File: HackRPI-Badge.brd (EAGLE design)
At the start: 124.5 x 94 mm, 41 parts, among them J1 FTDI_BASICPTH, J2 SOLDERJUMPERTRACE-PTH, U2 3.3V, U4 74595, U5 74595, U6 74595, U7 74165DT

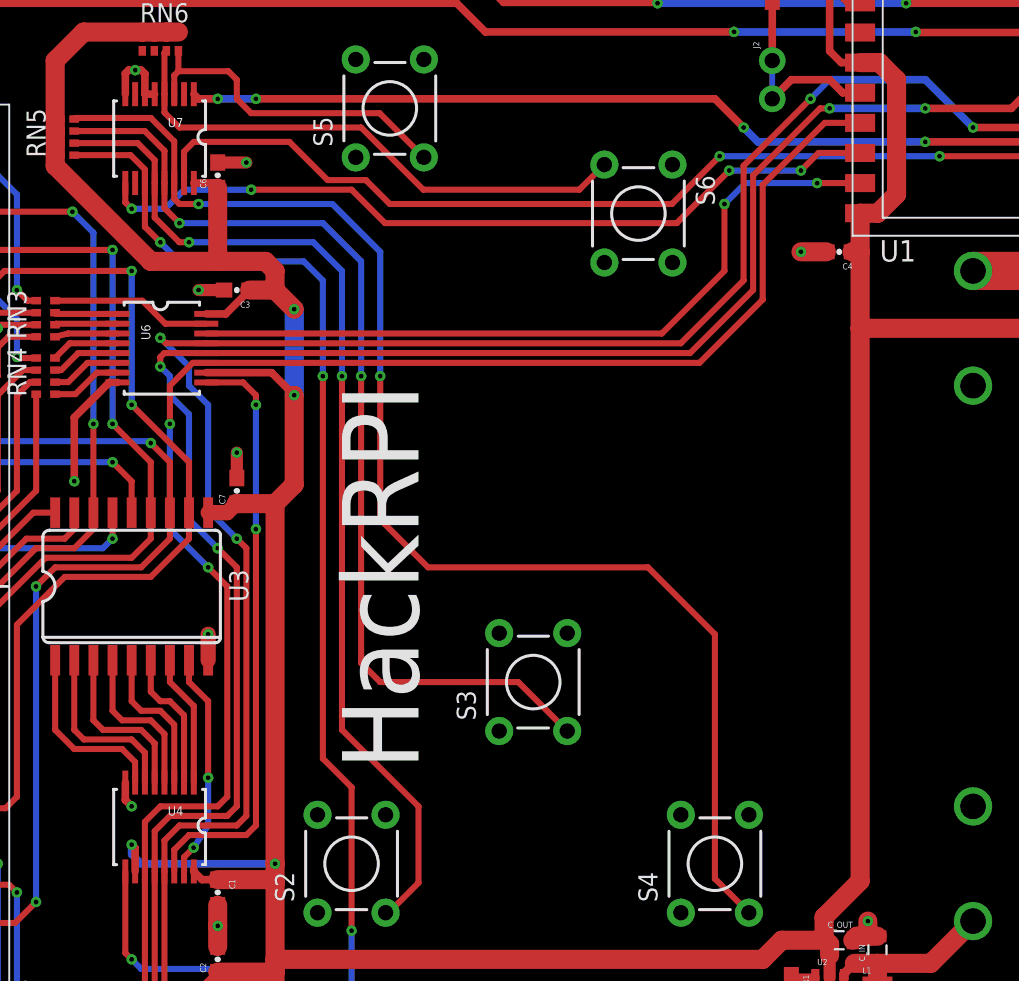
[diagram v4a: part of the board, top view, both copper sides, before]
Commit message: Added flash memory for storing certificates, named some nets to be more clear
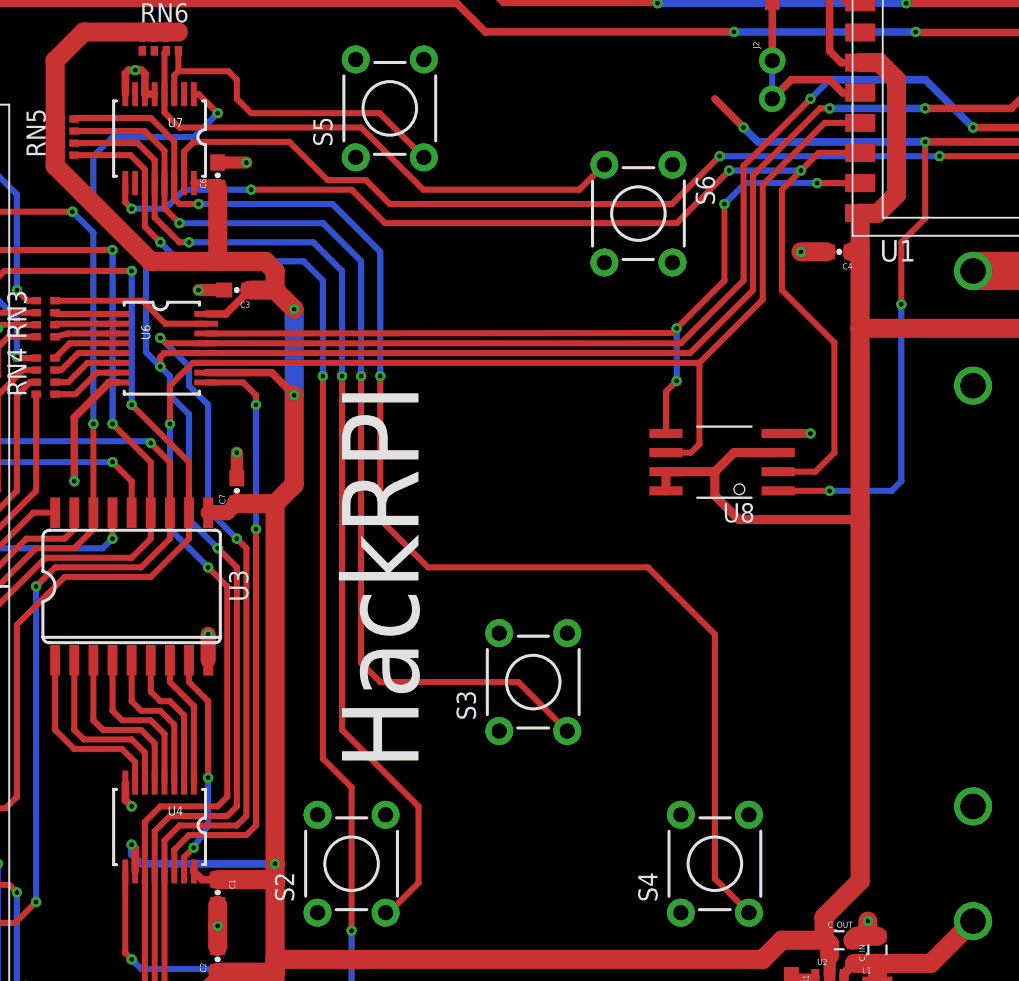
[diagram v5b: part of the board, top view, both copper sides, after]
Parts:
- added U8: AT25FS010, SparkFun-DigitalIC:SO08WIDE
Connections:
- net GPIO2 renamed INPUT_CS
- removed net GPIO0: R3.1, U1.12, U7.1
- new net FLASH_CS: R3.1, U1.12, U8.1
- net 3.3V: now also U8.3, U8.7, U8.8
- net GND: now also U8.4
- net LAT: now also U7.1
- net MISO: now also U8.2
- net MOSI: now also U8.5
- net SCK: now also U8.6
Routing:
- net GPIO0: track 64.9 -> 0.00 mm, vias 4 -> 0
- net FLASH_CS: track 0.00 -> 62.8 mm, vias 0 -> 4
- net LAT: track 128.7 -> 156.1 mm, vias 4 -> 5
- net MISO: track 53.6 -> 78.6 mm
- net 3.3V: track 284.5 -> 305.9 mm
- net SCK: track 111.1 -> 118.9 mm
- net MOSI: track 50.2 -> 57.8 mm, vias 2 -> 4
- net GND: track 36.6 -> 38.7 mm, vias 13 -> 14
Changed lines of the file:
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@@
 <attribute name="PROD_ID" value="BATT-08571" x="116.84" y="45.72" size="1.778" layer="28" rot="MR270" display="off"/>
 </element>
+<element name="U8" library="SparkFun-DigitalIC" package="SO08WIDE" value="AT25FS010" x="91.44" y="54.61" rot="R90"/>
 </elements>
 <signals>
@@
 <wire x1="54.61" y1="59.69" x2="56.125" y2="61.205" width="0.4064" layer="1"/>
 <wire x1="56.125" y1="61.205" x2="57.025" y2="61.205" width="0.4064" layer="1"/>
+<contactref element="U8" pad="6"/>
+<wire x1="87.5538" y1="55.245" x2="89.2175" y2="55.245" width="0.4064" layer="1"/>
+<wire x1="89.78" y1="61.205" x2="89.78" y2="55.8075" width="0.4064" layer="1"/>
+<wire x1="89.78" y1="55.8075" x2="89.2175" y2="55.245" width="0.4064" layer="1"/>
 </signal>
 <signal name="MISO">
@@
 <wire x1="96.52" y1="73.9775" x2="97.6875" y2="75.145" width="0.4064" layer="1"/>
 <wire x1="97.6875" y1="75.145" x2="100.45" y2="75.145" width="0.4064" layer="1"/>
+<contactref element="U8" pad="2"/>
+<wire x1="95.0087" y1="53.975" x2="97.4725" y2="53.975" width="0.4064" layer="1"/>
+<wire x1="97.4725" y1="53.975" x2="98.7425" y2="55.245" width="0.4064" layer="1"/>
+<wire x1="98.7425" y1="55.245" x2="98.7425" y2="62.5475" width="0.4064" layer="1"/>
+<wire x1="98.7425" y1="62.5475" x2="95.25" y2="66.04" width="0.4064" layer="1"/>
+<wire x1="95.25" y1="66.04" x2="95.25" y2="72.7075" width="0.4064" layer="1"/>
+<wire x1="95.25" y1="72.7075" x2="96.52" y2="73.9775" width="0.4064" layer="1"/>
 </signal>
 <signal name="MOSI">
 <contactref element="U1" pad="7"/>
 <contactref element="U6" pad="14"/>
-<wire x1="57.025" y1="63.155" x2="87.285" y2="63.155" width="0.4064" layer="1"/>
-<wire x1="87.285" y1="63.155" x2="91.44" y2="67.31" width="0.4064" layer="1"/>
-<wire x1="91.44" y1="67.31" x2="91.44" y2="71.755" width="0.4064" layer="1"/>
+<wire x1="57.025" y1="63.155" x2="87.9475" y2="63.1825" width="0.4064" layer="1"/>
+<wire x1="87.9475" y1="63.1825" x2="88.265" y2="63.5" width="0.4064" layer="1"/>
+<wire x1="88.265" y1="63.5" x2="91.44" y2="66.675" width="0.4064" layer="1"/>
+<wire x1="91.44" y1="66.675" x2="91.44" y2="71.755" width="0.4064" layer="1"/>
 <via x="91.44" y="71.755" extent="1-16" drill="0.3048"/>
 <wire x1="91.44" y1="71.755" x2="92.83" y2="73.145" width="0.4064" layer="16"/>
@@
 <via x="97.5925" y="73.145" extent="1-16" drill="0.3048"/>
 <wire x1="97.5925" y1="73.145" x2="92.83" y2="73.145" width="0.4064" layer="16"/>
+<contactref element="U8" pad="5"/>
+<wire x1="87.5538" y1="59.2963" x2="87.5538" y2="56.515" width="0.4064" layer="1"/>
+<wire x1="88.265" y1="63.5" x2="88.265" y2="60.0075" width="0.4064" layer="16"/>
+<via x="88.265" y="60.0075" extent="1-16" drill="0.3048"/>
+<wire x1="88.265" y1="60.0075" x2="87.5538" y2="59.2963" width="0.4064" layer="1"/>
+<via x="88.265" y="63.5" extent="1-16" drill="0.3048"/>
 </signal>
 <signal name="3.3V" class="1">
@@
 <wire x1="98.425" y1="21.855" x2="98.425" y2="20.3501" width="0.8128" layer="1"/>
 <wire x1="98.055" y1="24.395" x2="100.45" y2="26.79" width="1.27" layer="1"/>
-<wire x1="100.45" y1="26.79" x2="100.45" y2="63.5" width="1.27" layer="1"/>
+<wire x1="100.45" y1="26.79" x2="100.45" y2="50.4825" width="1.27" layer="1"/>
+<wire x1="100.45" y1="50.4825" x2="100.45" y2="63.5" width="1.27" layer="1"/>
 <wire x1="100.45" y1="63.5" x2="100.45" y2="68.58" width="1.27" layer="1"/>
 <wire x1="100.45" y1="68.58" x2="100.45" y2="71.145" width="1.27" layer="1"/>
@@
 <wire x1="57.025" y1="60.555" x2="61.365" y2="60.555" width="0.508" layer="1"/>
 <wire x1="61.365" y1="60.555" x2="62.865" y2="59.055" width="0.508" layer="1"/>
+<contactref element="U8" pad="3"/>
+<contactref element="U8" pad="8"/>
+<contactref element="U8" pad="7"/>
+<wire x1="87.5538" y1="52.705" x2="87.5538" y2="53.975" width="0.6096" layer="1"/>
+<wire x1="87.5538" y1="53.975" x2="90.805" y2="53.975" width="0.6096" layer="1"/>
+<wire x1="95.0087" y1="55.245" x2="92.075" y2="55.245" width="0.6096" layer="1"/>
+<wire x1="92.075" y1="55.245" x2="90.805" y2="53.975" width="0.6096" layer="1"/>
+<wire x1="90.805" y1="53.975" x2="90.805" y2="52.3875" width="0.6096" layer="1"/>
+<wire x1="90.805" y1="52.3875" x2="92.3925" y2="50.8" width="0.6096" layer="1"/>
+<wire x1="100.45" y1="50.8" x2="92.3925" y2="50.8" width="0.6096" layer="1"/>
+<wire x1="100.45" y1="50.8" x2="100.45" y2="50.4825" width="0.6096" layer="1"/>
 </signal>
 <signal name="GND" class="1">
@@
 <wire x1="48.26" y1="57.58" x2="48.26" y2="53.34" width="0.508" layer="1"/>
 <via x="48.26" y="53.34" extent="1-16" drill="0.3048"/>
-</signal>
-<signal name="GPIO2">
+<contactref element="U8" pad="4"/>
+<wire x1="95.0087" y1="56.515" x2="97.155" y2="56.515" width="0.6096" layer="1"/>
+<via x="97.155" y="56.515" extent="1-16" drill="0.3048"/>
+</signal>
+<signal name="INPUT_CS">
 <contactref element="U1" pad="11"/>
 <contactref element="R4" pad="1"/>
-<contactref element="U7" pad="15"/>
 <wire x1="115.45" y1="75.145" x2="118.95" y2="75.145" width="0.8128" layer="1"/>
 <wire x1="118.95" y1="75.145" x2="119.165" y2="74.93" width="0.8128" layer="1"/>
-<wire x1="55.55" y1="73.15" x2="55.55" y2="75.235" width="0.4064" layer="1"/>
 <wire x1="55.55" y1="75.235" x2="56.1975" y2="75.8825" width="0.4064" layer="1"/>
 <wire x1="56.1975" y1="75.8825" x2="62.5475" y2="75.8825" width="0.4064" layer="1"/>
@@
 <wire x1="112.395" y1="74.93" x2="112.61" y2="75.145" width="0.4064" layer="1"/>
 <wire x1="112.61" y1="75.145" x2="115.45" y2="75.145" width="0.4064" layer="1"/>
-</signal>
-<signal name="GPIO0">
+<contactref element="U7" pad="15"/>
+<wire x1="55.55" y1="75.235" x2="55.55" y2="73.15" width="0.4064" layer="1"/>
+</signal>
+<signal name="FLASH_CS">
 <contactref element="U1" pad="12"/>
 <contactref element="R3" pad="1"/>
-<contactref element="U7" pad="1"/>
-<wire x1="56.51" y1="78.74" x2="57.785" y2="78.74" width="0.508" layer="1"/>
-<via x="57.785" y="78.74" extent="1-16" drill="0.3048"/>
-<wire x1="57.785" y1="78.74" x2="60.325" y2="78.74" width="0.508" layer="16"/>
-<via x="60.325" y="78.74" extent="1-16" drill="0.3048"/>
-<wire x1="60.325" y1="78.74" x2="90.805" y2="78.74" width="0.508" layer="1"/>
 <wire x1="90.805" y1="78.74" x2="92.71" y2="76.835" width="0.508" layer="1"/>
 <via x="92.71" y="76.835" extent="1-16" drill="0.3048"/>
 <wire x1="92.71" y1="76.835" x2="93.6625" y2="75.8825" width="0.508" layer="16"/>
-<wire x1="93.6625" y1="75.8825" x2="104.775" y2="75.8825" width="0.508" layer="16"/>
+<wire x1="93.6625" y1="75.8825" x2="96.2025" y2="75.8825" width="0.508" layer="16"/>
 <via x="104.775" y="75.8825" extent="1-16" drill="0.3048"/>
+<wire x1="96.2025" y1="75.8825" x2="104.775" y2="75.8825" width="0.508" layer="16"/>
 <wire x1="104.775" y1="75.8825" x2="112.0775" y2="75.8825" width="0.508" layer="1"/>
 <wire x1="112.0775" y1="75.8825" x2="113.34" y2="77.145" width="0.508" layer="1"/>
@@
 <wire x1="119.165" y1="77.47" x2="118.84" y2="77.145" width="0.8128" layer="1"/>
 <wire x1="118.84" y1="77.145" x2="115.45" y2="77.145" width="0.8128" layer="1"/>
-<wire x1="56.51" y1="78.74" x2="56.2" y2="79.05" width="0.508" layer="1"/>
+<contactref element="U8" pad="1"/>
+<wire x1="95.25" y1="75.8825" x2="96.2025" y2="75.8825" width="0.4064" layer="16"/>
+<wire x1="95.0087" y1="52.705" x2="98.425" y2="52.705" width="0.4064" layer="1"/>
+<via x="98.425" y="52.705" extent="1-16" drill="0.3048"/>
+<wire x1="98.425" y1="52.705" x2="102.5525" y2="52.705" width="0.4064" layer="16"/>
+<wire x1="102.5525" y1="52.705" x2="103.1875" y2="53.34" width="0.4064" layer="16"/>
+<wire x1="103.1875" y1="53.34" x2="103.1875" y2="65.0875" width="0.4064" layer="16"/>
+<via x="103.1875" y="65.0875" extent="1-16" drill="0.3048"/>
+<wire x1="103.1875" y1="65.0875" x2="103.1875" y2="69.215" width="0.4064" layer="1"/>
+<wire x1="103.1875" y1="69.215" x2="104.775" y2="70.8025" width="0.4064" layer="1"/>
+<wire x1="104.775" y1="70.8025" x2="104.775" y2="75.8825" width="0.4064" layer="1"/>
 </signal>
 <signal name="V_BATT" class="1">
@@
 <wire x1="53.975" y1="61.595" x2="54.235" y2="61.855" width="0.4064" layer="1"/>
 <wire x1="54.235" y1="61.855" x2="57.025" y2="61.855" width="0.4064" layer="1"/>
+<contactref element="U7" pad="1"/>
+<wire x1="56.2" y1="79.05" x2="56.5225" y2="79.05" width="0.4064" layer="1"/>
+<wire x1="56.5225" y1="79.05" x2="57.785" y2="77.7875" width="0.4064" layer="1"/>
+<via x="57.785" y="77.7875" extent="1-16" drill="0.3048"/>
+<wire x1="57.785" y1="77.7875" x2="56.1975" y2="76.2" width="0.4064" layer="16"/>
+<wire x1="56.1975" y1="76.2" x2="50.8" y2="76.2" width="0.4064" layer="16"/>
+<wire x1="50.8" y1="76.2" x2="49.53" y2="74.93" width="0.4064" layer="16"/>
+<wire x1="49.53" y1="74.93" x2="49.53" y2="71.755" width="0.4064" layer="16"/>
+<wire x1="49.53" y1="71.755" x2="53.0225" y2="68.2625" width="0.4064" layer="16"/>
+<wire x1="53.0225" y1="68.2625" x2="53.0225" y2="61.9125" width="0.4064" layer="16"/>
+<wire x1="53.0225" y1="61.9125" x2="53.975" y2="60.96" width="0.4064" layer="16"/>
 </signal>
 <signal name="OE">

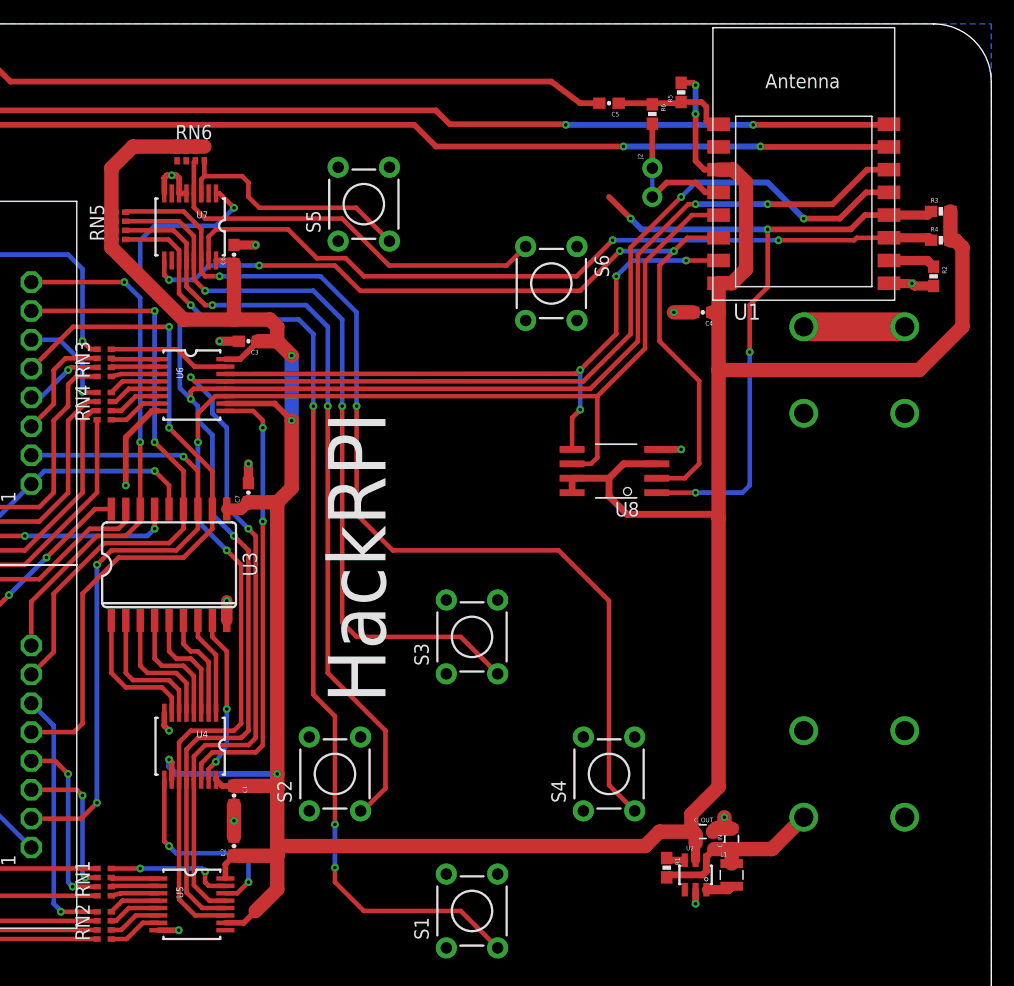
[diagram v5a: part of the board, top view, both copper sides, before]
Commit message: Fixed 74165 sck pin connection, updated gitignore to ignore lock files
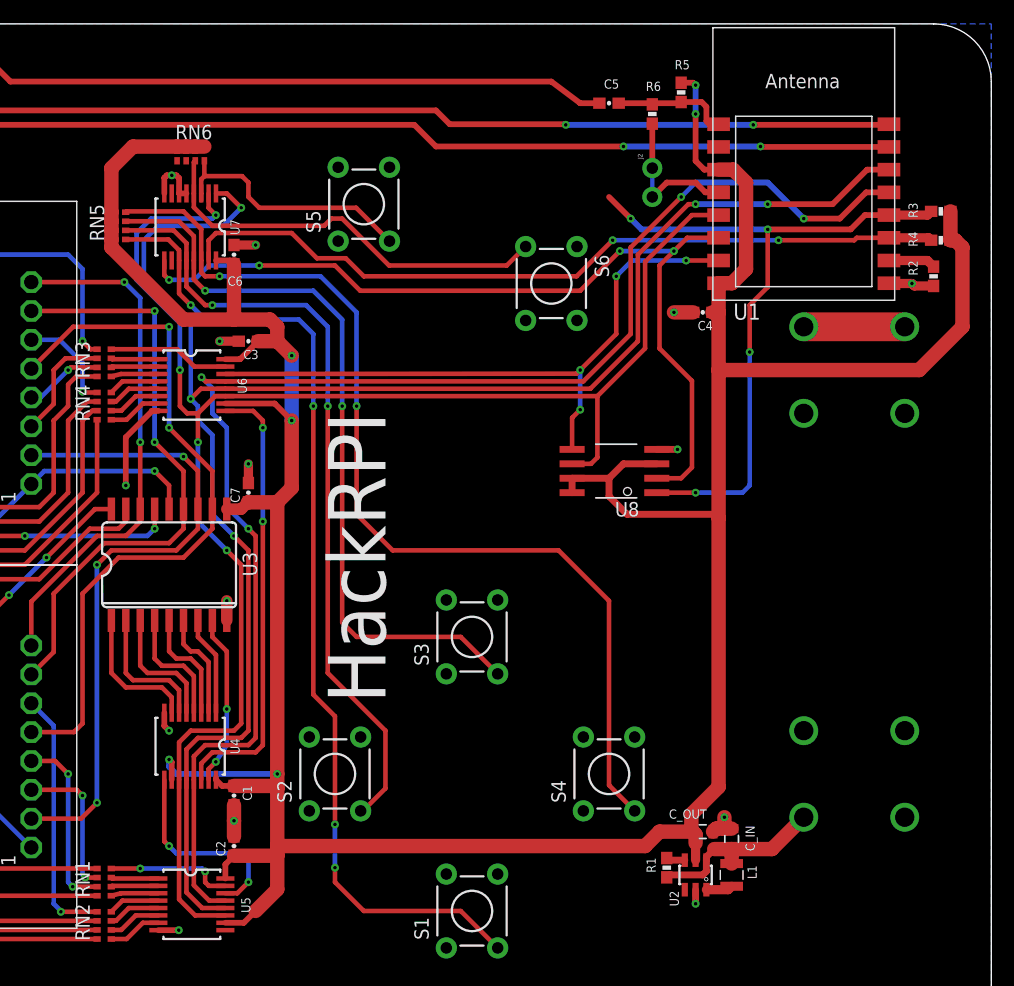
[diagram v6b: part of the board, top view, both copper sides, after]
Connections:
- removed net CLK: U7.2
- net SCK: now also U7.2
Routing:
- net SCK: track 118.9 -> 147.4 mm, vias 2 -> 4
- net OE: track 130.5 -> 129.2 mm
- net MISO: track 78.6 -> 77.9 mm
- net B: track 36.2 -> 36.7 mm
